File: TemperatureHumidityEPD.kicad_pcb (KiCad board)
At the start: 2 copper layers, 48 x 33 mm, 25 parts, among them J1 Conn_01x08, J2 Conn_01x05, J3 Conn_01x02, Q1 IRLML6344, U1 STM32L031Fx, U2 SI7021

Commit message: Edits of the schematic, porting the design to MAX32660.
Full part number information added in the schematic.

Footprints linked. However, two parts need new footprints: 68uH inductor and the SWD debug connector.
Related to this TODO: final check of the FPC connector.

Group review of the schematic is now in progress.
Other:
- net class 0.2mm removed
- net class Default removed
- net class Minimal removed
- net class Power removed

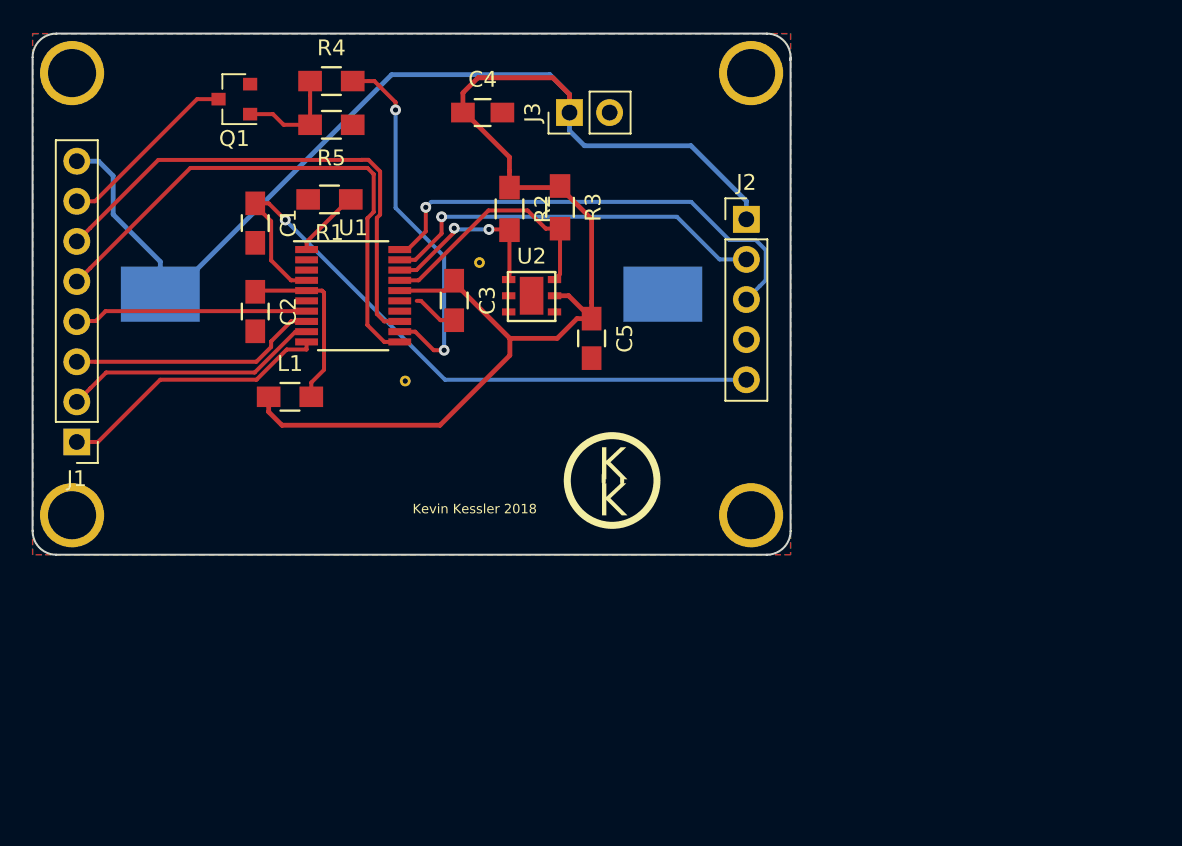
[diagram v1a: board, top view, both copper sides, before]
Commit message: Completely finished layout. Various small schematic tweaks along the way of layout.
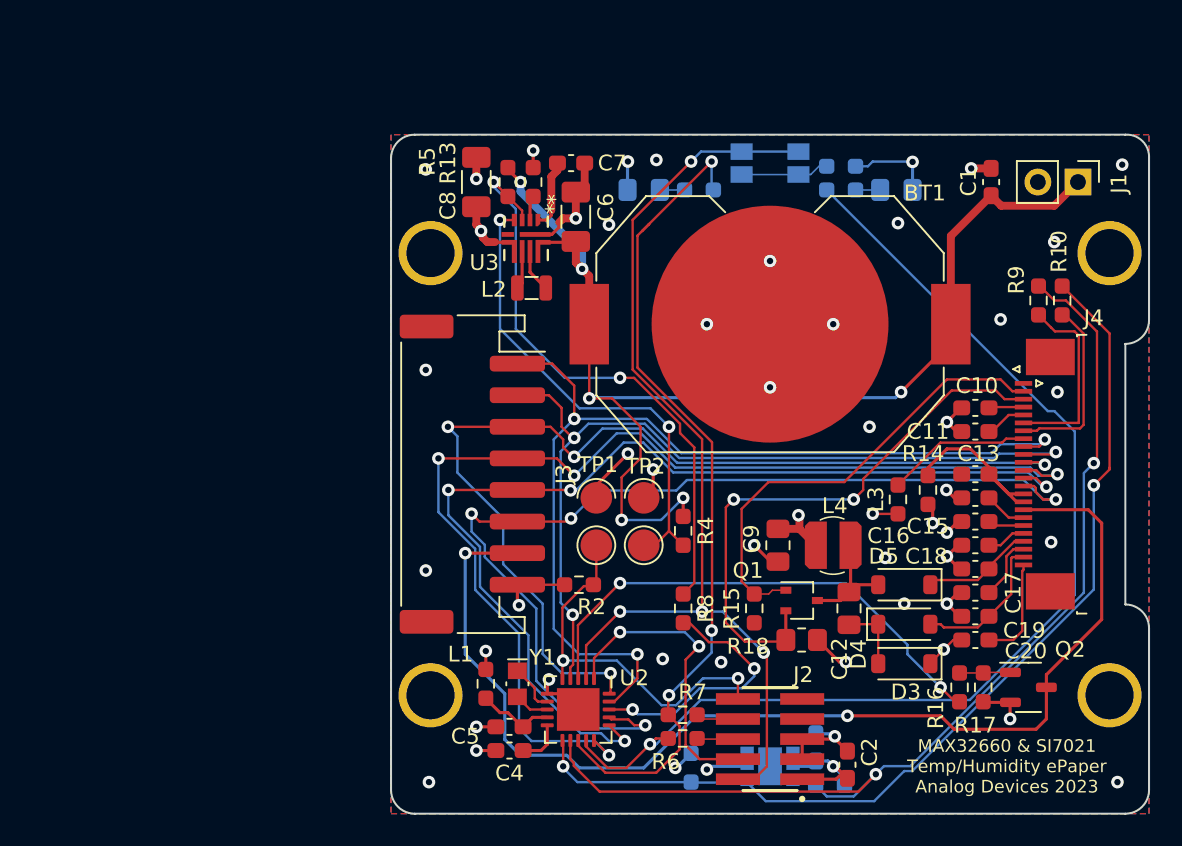
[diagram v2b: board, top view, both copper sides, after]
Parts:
- removed REF** (x2): VIA_13MIL, KevinLibrary:VIA_13MIL
- removed REF**: Logo, KevinLibrary:Logo
- added C10: 10u, Capacitor_SMD:C_0603_1608Metric_Pad1.08x0.95mm_HandSolder, F.Cu at (159.7, 103.7)
- added C11: 10u, Capacitor_SMD:C_0603_1608Metric_Pad1.08x0.95mm_HandSolder, F.Cu at (159.7, 105.2)
- added C12: 4.7u, Capacitor_SMD:C_0805_2012Metric_Pad1.18x1.45mm_HandSolder, F.Cu at (151.7, 116.4)
- added C13: 1u, Capacitor_SMD:C_0603_1608Metric_Pad1.08x0.95mm_HandSolder, F.Cu at (159.7, 107.9)
- added C14: 10u, Capacitor_SMD:C_0603_1608Metric_Pad1.08x0.95mm_HandSolder, F.Cu at (159.7, 109.4)
- added C15: 10u, Capacitor_SMD:C_0603_1608Metric_Pad1.08x0.95mm_HandSolder, F.Cu at (159.7, 110.9)
- added C16: 10u, Capacitor_SMD:C_0603_1608Metric_Pad1.08x0.95mm_HandSolder, F.Cu at (159.7, 112.4)
- added C17: 10u, Capacitor_SMD:C_0603_1608Metric_Pad1.08x0.95mm_HandSolder, F.Cu at (159.7, 113.9)
- added C18: 10u, Capacitor_SMD:C_0603_1608Metric_Pad1.08x0.95mm_HandSolder, F.Cu at (159.7, 115.4)
- added C19: 10u, Capacitor_SMD:C_0603_1608Metric_Pad1.08x0.95mm_HandSolder, F.Cu at (159.7, 116.9)
- added C20: 10u, Capacitor_SMD:C_0603_1608Metric_Pad1.08x0.95mm_HandSolder, F.Cu at (159.7, 118.4)
- added C6: 22u, Capacitor_SMD:C_1206_3216Metric_Pad1.33x1.80mm_HandSolder, F.Cu at (134.4, 91.6)
- added C7: 22p, Capacitor_SMD:C_0603_1608Metric_Pad1.08x0.95mm_HandSolder, F.Cu at (134.1, 88.2)
- added C8: 22u, Capacitor_SMD:C_1206_3216Metric_Pad1.33x1.80mm_HandSolder, F.Cu at (128.1, 89.4)
- added C9: 4.7u, Capacitor_SMD:C_0805_2012Metric_Pad1.18x1.45mm_HandSolder, F.Cu at (147.2, 112.4)
- added D1: LED, LED_SMD:LED_0805_2012Metric_Pad1.15x1.40mm_HandSolder, B.Cu at (154.7, 89.9)
- added D2: LED, LED_SMD:LED_0805_2012Metric_Pad1.15x1.40mm_HandSolder, B.Cu at (138.7, 89.9)
- added D3: MBR0530, Diode_SMD:D_SOD-123, F.Cu at (155.2, 119.9)
- added D4: MBR0530, Diode_SMD:D_SOD-123, F.Cu at (155.2, 117.4)
- added D5: MBR0530, Diode_SMD:D_SOD-123, F.Cu at (155.2, 114.9)
- added J4: Conn_01x24, Connectors_Custom:TE_2-1734839-4_1x24-1MP_P0.5mm_Horizontal_reversednumber, F.Cu at (164.1, 107.9)
- added L2: 1u, Inductors_Custom:L_0805_2016Metric, F.Cu at (131.6, 96.1)
- added L3: 0, Resistor_SMD:R_0603_1608Metric_Pad0.98x0.95mm_HandSolder, F.Cu at (156.7, 108.9)
- added L4: 68u, Inductors_Custom:L_3x3_H3, F.Cu at (150.7, 112.4)
- added Q2: IRLML6344, Package_TO_SOT_SMD:SOT-23-3, F.Cu at (163.1, 121.4)
- added R10: 0, Resistor_SMD:R_0603_1608Metric_Pad0.98x0.95mm_HandSolder, F.Cu at (165.2, 96.9)
- added R11: 56, Resistor_SMD:R_0603_1608Metric_Pad0.98x0.95mm_HandSolder, B.Cu at (151.2, 89.9)
- added R12: 56, Resistor_SMD:R_0603_1608Metric_Pad0.98x0.95mm_HandSolder, B.Cu at (142.2, 89.9)
- added R13: DNP, Resistor_SMD:R_0603_1608Metric_Pad0.98x0.95mm_HandSolder, F.Cu at (131.7, 89.4)
- added R14: 0, Resistor_SMD:R_0603_1608Metric_Pad0.98x0.95mm_HandSolder, F.Cu at (154.8, 109.5)
- added R15: 10K, Resistor_SMD:R_0603_1608Metric_Pad0.98x0.95mm_HandSolder, F.Cu at (145.7, 116.4)
- added R16: 100R, Resistor_SMD:R_0603_1608Metric_Pad0.98x0.95mm_HandSolder, F.Cu at (158.7, 121.4)
- added R17: 100K, Resistor_SMD:R_0603_1608Metric_Pad0.98x0.95mm_HandSolder, F.Cu at (160.2, 121.4)
- added R18: 0R47, Resistor_SMD:R_0805_2012Metric_Pad1.20x1.40mm_HandSolder, F.Cu at (148.7, 118.4)
- added R19: 10K, Resistor_SMD:R_0603_1608Metric_Pad0.98x0.95mm_HandSolder, B.Cu at (151.2, 88.4)
- added R6: 1k, Resistor_SMD:R_0603_1608Metric_Pad0.98x0.95mm_HandSolder, F.Cu at (141.2, 124.6)
- added R7: 1k, Resistor_SMD:R_0603_1608Metric_Pad0.98x0.95mm_HandSolder, F.Cu at (141.2, 123.1)
- added R8: 100R, Resistor_SMD:R_0603_1608Metric_Pad0.98x0.95mm_HandSolder, F.Cu at (141.2, 116.4)
- added R9: 0, Resistor_SMD:R_0603_1608Metric_Pad0.98x0.95mm_HandSolder, F.Cu at (163.7, 96.9)
- added SW1: SW_Push, Switch_Custom:Panasonic_EVQPUJ_EVQPUA, B.Cu at (146.7, 88.2)
- added TP1: TestPoint_2Pole, Connectors_Custom:TestPoint_Padx2_D2.0mm, F.Cu at (135.7, 110.9)
- added TP2: TestPoint_2Pole, Connectors_Custom:TestPoint_Padx2_D2.0mm, F.Cu at (138.7, 110.9)
- added U3: MAX20343H, ADI_Power:MAX20343H, F.Cu at (131.2, 93.0)
- added Y1: 32.7680KHZ, Crystal:Crystal_SMD_MicroCrystal_CM9V-T1A-2Pin_1.6x1.0mm_HandSoldering, F.Cu at (130.7, 121.2)
- BT1: value Battery_Cell -> CR2032; footprint KevinLibrary:CR2032_BATTERY_HOLDER -> Connectors_Custom:BatteryHolder_TE_BATT-HLD-000_1x2032; moved to F.Cu
- C1: value 100n -> 10u; footprint Capacitors_SMD:C_0805_HandSoldering -> Capacitor_SMD:C_0603_1608Metric_Pad1.08x0.95mm_HandSolder
- C2, C5: value 100n -> 1u; footprint Capacitors_SMD:C_0805_HandSoldering -> Capacitor_SMD:C_0603_1608Metric_Pad1.08x0.95mm_HandSolder
- C3: footprint Capacitors_SMD:C_0805_HandSoldering -> Capacitor_SMD:C_0603_1608Metric_Pad1.08x0.95mm_HandSolder; moved to B.Cu
- C4: value 10u -> 1u; footprint Capacitors_SMD:C_0805_HandSoldering -> Capacitor_SMD:C_0603_1608Metric_Pad1.08x0.95mm_HandSolder
- J1: value Conn_01x08 -> Conn_01x02; footprint Pin_Headers:Pin_Header_Straight_1x08_Pitch2.54mm -> Connectors_Custom:Pin_Header_Straight_1x02_Pitch2.54mm
- J2: value Conn_01x05 -> FTSH-105-01-L-DV-K; footprint Pin_Headers:Pin_Header_Straight_1x05_Pitch2.54mm -> Connectors_Custom:SAMTEC_FTSH-105-01-L-DV-K
- J3: value Conn_01x02 -> Conn_01x08; footprint Pin_Headers:Pin_Header_Straight_1x02_Pitch2.54mm -> Connector_JST:JST_PH_S8B-PH-SM4-TB_1x08-1MP_P2.00mm_Horizontal
- L1: value 600Ohm -> 0; footprint Resistors_SMD:R_0805_HandSoldering -> Resistor_SMD:R_0603_1608Metric_Pad0.98x0.95mm_HandSolder
- MP1, MP2, MP3, MP4: footprint KevinLibrary:TH-M3 -> Connectors_Custom:TH-M3
- Q1: value IRLML6344 -> Si1308EDL; footprint TO_SOT_Packages_SMD:SOT-23 -> Package_TO_SOT_SMD:SOT-323_SC-70
- R1, R3: footprint Resistors_SMD:R_0805_HandSoldering -> Resistor_SMD:R_0603_1608Metric_Pad0.98x0.95mm_HandSolder; moved to B.Cu
- R2: footprint Resistors_SMD:R_0805_HandSoldering -> Resistor_SMD:R_0603_1608Metric_Pad0.98x0.95mm_HandSolder
- R4: value 100R -> 10K; footprint Resistors_SMD:R_0805_HandSoldering -> Resistor_SMD:R_0603_1608Metric_Pad0.98x0.95mm_HandSolder
- R5: value 100K -> 10K; footprint Resistors_SMD:R_0805_HandSoldering -> Resistor_SMD:R_0603_1608Metric_Pad0.98x0.95mm_HandSolder
- U1: value STM32L031Fx -> SI7021; footprint Housings_SSOP:TSSOP-20_4.4x6.5mm_Pitch0.65mm -> Silabs_custom:SI7021; moved to B.Cu
- U2: value SI7021 -> MAX32660GTP; footprint KevinLibrary:SI7021 -> Package_DFN_QFN:TQFN-20-1EP_4x4mm_P0.5mm_EP2.7x2.7mm
- moved J1 65.5 mm to (166.2, 89.4), turned to -90 degrees
- moved Q1 47.9 mm to (148.7, 115.9), turned to 0 degrees
- moved C2 47.2 mm to (151.6, 126.3), turned to 90 degrees
- moved C1 46.7 mm to (160.7, 89.4), turned to 90 degrees
- moved R1 42.7 mm to (141.7, 126.5), turned to -90 degrees
- moved C4 40.4 mm to (130.2, 125.4), turned to 180 degrees
- moved R3 40.4 mm to (150.5, 127.6), turned to 180 degrees
- moved U1 39.8 mm to (146.7, 126.4)
- moved C3 36.4 mm to (149.6, 125.2), turned to 90 degrees
- moved R4 36.2 mm to (141.2, 111.5), turned to -90 degrees
- moved J2 32.9 mm to (146.7, 124.7), turned to 90 degrees
- moved U2 26.4 mm to (134.6, 122.8), turned to -90 degrees
- moved MP2 25.4 mm to (125.2, 93.9)
- moved MP3 25.4 mm to (125.2, 121.9)
- moved MP1 25.4 mm to (168.2, 121.9)
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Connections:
- BT1 pad 1: +3V3 -> +BATT
- BT1 pad 2: GND -> +BATT
- C1 pad 1: /NRST -> +BATT
- C2 pad 1: Net-(C2-Pad1) -> +3V3
- C4 pad 1: +3V3 -> /VCORE
- C5 pad 1: +3V3 -> /VDD
- J1 pad 1: /BUSY -> +BATT
- J1 pad 2: /RST -> GND
- J3 pad 1: +3V3 -> /EPD_BUSY
- J3 pad 2: GND -> /EPD_RST
- L1 pad 1: +3V3 -> /VDD
- L1 pad 2: Net-(C2-Pad1) -> +3V3
- Q1 pad 1: Net-(Q1-Pad1) -> /GDR
- Q1 pad 2: GND -> /RESE
- Q1 pad 3: /EPD_GND -> Net-(D5-A)
- R1 pad 1: Net-(R1-Pad1) -> +3V3
- R1 pad 2: GND -> /I2C0_SDA
- R2 pad 2: /SDA -> /MCU_RESET
- R3 pad 2: /SCL -> /I2C0_SCL
- R4 pad 1: Net-(Q1-Pad1) -> +BATT
- R4 pad 2: /EPD_POWER -> Net-(U3-EN)
- R5 pad 1: GND -> +BATT
- R5 pad 2: Net-(Q1-Pad1) -> Net-(U3-INGOOD)
- U1 pad 1: Net-(R1-Pad1) -> /I2C0_SDA
- U1 pad 3: GND -> unconnected-(U1-NC-Pad3)
- U1 pad 4: /NRST -> unconnected-(U1-NC-Pad4)
- U1 pad 5: Net-(C2-Pad1) -> +3V3
- U1 pad 6: GND -> /I2C0_SCL
- U2 pad 1: /SDA -> /SWDCLK
- U2 pad 2: GND -> /SWDIO
- U2 pad 3: (no net) -> /EPD_POWER
- U2 pad 4: (no net) -> /EPD_RST
- U2 pad 5: +3V3 -> /MCU_RESET
- U2 pad 6: /SCL -> GND
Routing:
- net +3V3: track 125.6 -> 32.2 mm, vias 0 -> 9
- net +BATT: track 0.00 -> 77.8 mm, vias 0 -> 6
- net /SPI0_SS: track 0.00 -> 70.9 mm, vias 0 -> 4
- net /UART1_TX: track 0.00 -> 70.1 mm, vias 0 -> 1
- net /I2C0_SCL: track 0.00 -> 67.9 mm, vias 0 -> 2
- net /SPI0_SCLK: track 0.00 -> 65.1 mm, vias 0 -> 4
- net /EPD_DC: track 0.00 -> 65.0 mm, vias 0 -> 4
- net /SPI0_MOSI: track 0.00 -> 64.4 mm, vias 0 -> 4
- net /I2C0_SDA: track 0.00 -> 62.7 mm, vias 0 -> 2
- net /EPD_BUSY: track 0.00 -> 62.5 mm, vias 0 -> 3
- net /EPD_GND: track 11.7 -> 72.3 mm, vias 0 -> 2
- net /EPD_RST: track 0.00 -> 55.4 mm, vias 0 -> 3
- net /UART1_RX: track 0.00 -> 53.2 mm, vias 0 -> 3
- net GND: track 2.88 -> 52.5 mm, vias 0 -> 43
- net /NRST: track 42.5 -> 0.00 mm, vias 1 -> 0
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- added copper zone on In2.Cu, net +3V3
- added copper zone on In1.Cu, net GND
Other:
- board size 48 x 33 mm -> 48 x 43 mm
- copper layers 2 -> 4
- rule pad_to_mask_clearance: 0.05 -> 0
- board text added: "MAX32660 & SI7021 Temp/Humidity ePaper Analog Devices 2023"
- board text removed: "Kevin Kessler 2018"

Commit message: Fix backside silkscreen. Added outline of raw display. Regenerated fab files.
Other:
- board text added: "Raw ePaper Screen Adhere here"
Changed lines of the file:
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@@
     (grid_origin 122.7 129.4)
     (pcbplotparams
-      (layerselection 0x00010f8_ffffffff)
+      (layerselection 0x00010fc_ffffffff)
       (plot_on_all_layers_selection 0x0000000_00000000)
       (disableapertmacros false)
@@
     (property "Sheetname" "")
     (attr smd)
-    (fp_text reference "C3" (at 2.3 0.1 180) (layer "B.SilkS")
+    (fp_text reference "C3" (at 0.55 2.6 180) (layer "B.SilkS")
         (effects (font (size 1 1) (thickness 0.15)) (justify mirror))
     )
@@
     (property "Sheetname" "")
     (attr through_hole)
-    (fp_text reference "U1" (at 0.1 -2.3) (layer "B.SilkS")
+    (fp_text reference "U1" (at -3 -1.75) (layer "B.SilkS")
         (effects (font (size 1 1) (thickness 0.15)) (justify mirror))
     )
@@
     )
   )
+  (gr_line (start 165.36 92) (end 165.36 123.8)
+    (stroke (width 0.1) (type default)) (layer "B.SilkS"))
+  (gr_line (start 128.08 92) (end 128.08 123.8)
+    (stroke (width 0.1) (type default)) (layer "B.SilkS"))
+  (gr_line (start 150.7 123.8) (end 165.36 123.8)
+    (stroke (width 0.1) (type default)) (layer "B.SilkS"))
+  (gr_line (start 165.36 92) (end 128.08 92)
+    (stroke (width 0.1) (type default)) (layer "B.SilkS"))
+  (gr_line (start 128.08 123.8) (end 148.7 123.8)
+    (stroke (width 0.1) (type default)) (layer "B.SilkS"))
   (gr_line (start 165.36 92) (end 128.08 92)
     (stroke (width 0.1) (type default)) (layer "Dwgs.User"))
@@
     (effects (font (size 0.8 0.8) (thickness 0.127)) (justify mirror))
   )
+  (gr_text "Raw ePaper Screen\nAdhere here" (at 150.45 106.9) (layer "B.SilkS")
+    (effects (font (size 0.6 0.6) (thickness 0.127) bold) (justify left mirror))
+  )
   (gr_text "MAX32660 & SI7021 \nTemp/Humidity ePaper\nAnalog Devices 2023" (at 161.7 126.4) (layer "F.SilkS")
